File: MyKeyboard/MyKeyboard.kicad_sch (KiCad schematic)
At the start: 64 parts, among them J1 USB_C_Receptacle_USB2.0, J2 USB_C_Receptacle_USB2.0, J3 Conn_01x04, SW1 SW_Push, SW10 SW_Push, SW11 SW_Push, SW12 SW_Push, SW13 SW_Push, SW14 SW_Push, SW15 SW_Push, SW16 SW_Push, SW17 SW_Push, SW18 SW_Push, SW19 SW_Push, SW2 SW_Push, SW20 SW_Push, SW21 SW_Push, SW22 SW_Push, SW23 SW_Push, SW24 SW_Push, SW25 SW_Push, SW26 SW_Push, SW27 SW_Push, SW3 SW_Push, SW4 SW_Push, SW5 SW_Push, SW6 SW_Push, SW7 SW_Push, SW8 SW_Push, SW9 SW_Push, U1 E73-2G4M08S1C, U2 E73-2G4M08S1C

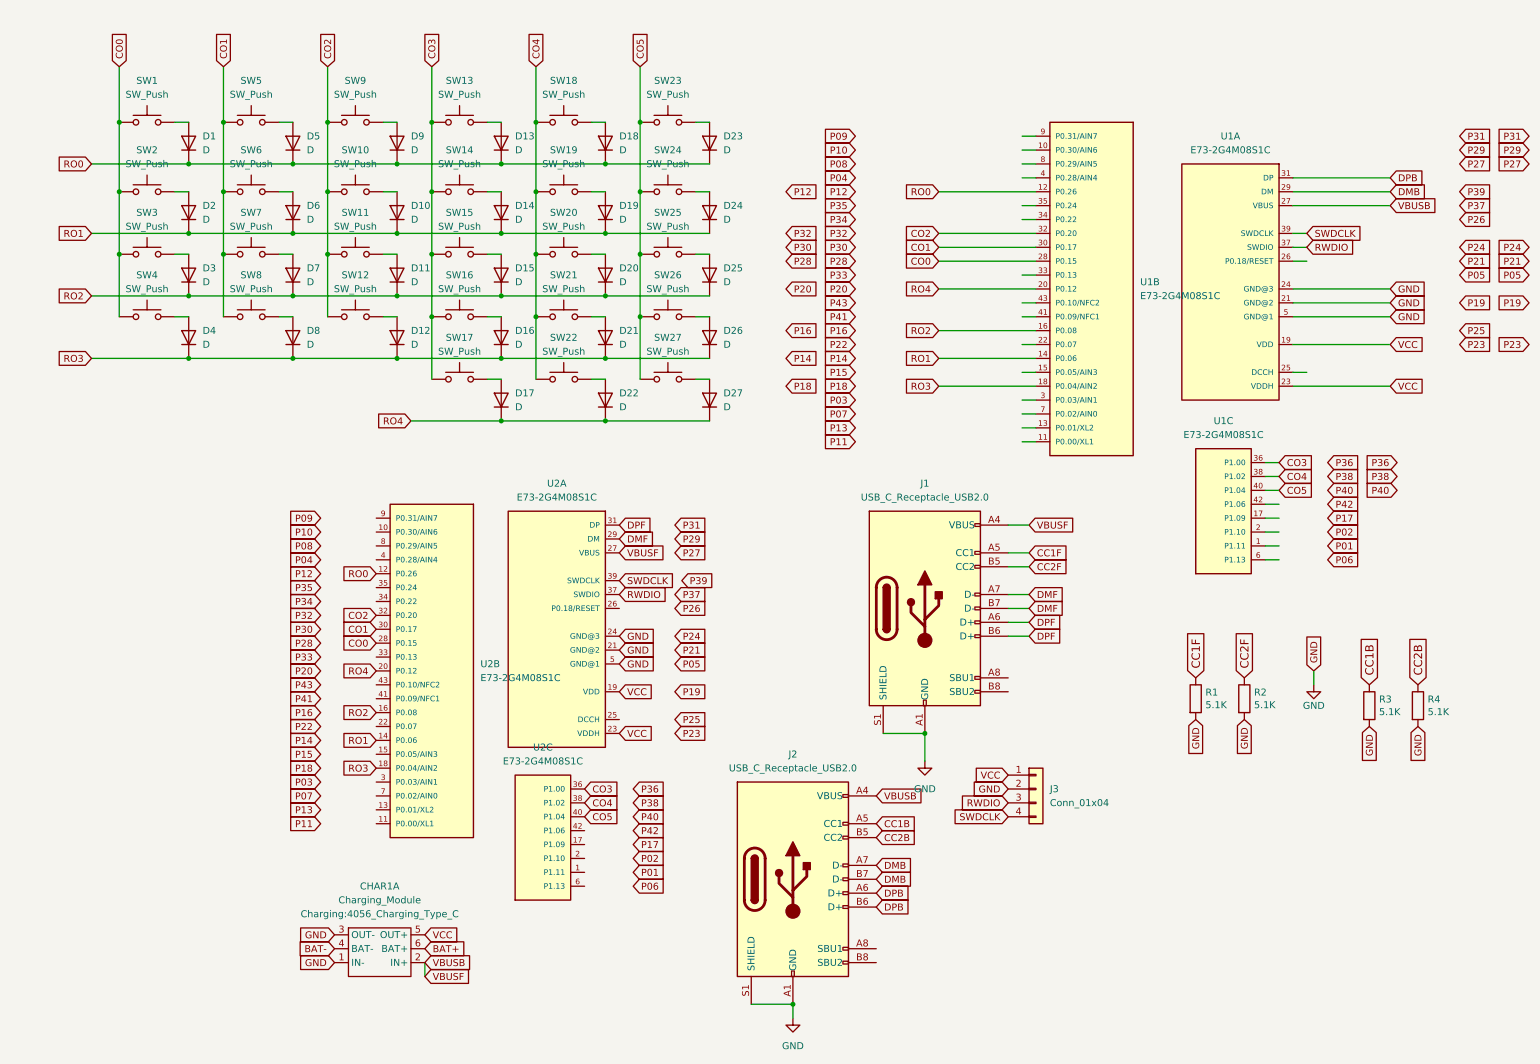
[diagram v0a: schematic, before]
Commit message: update reset btn and wiring
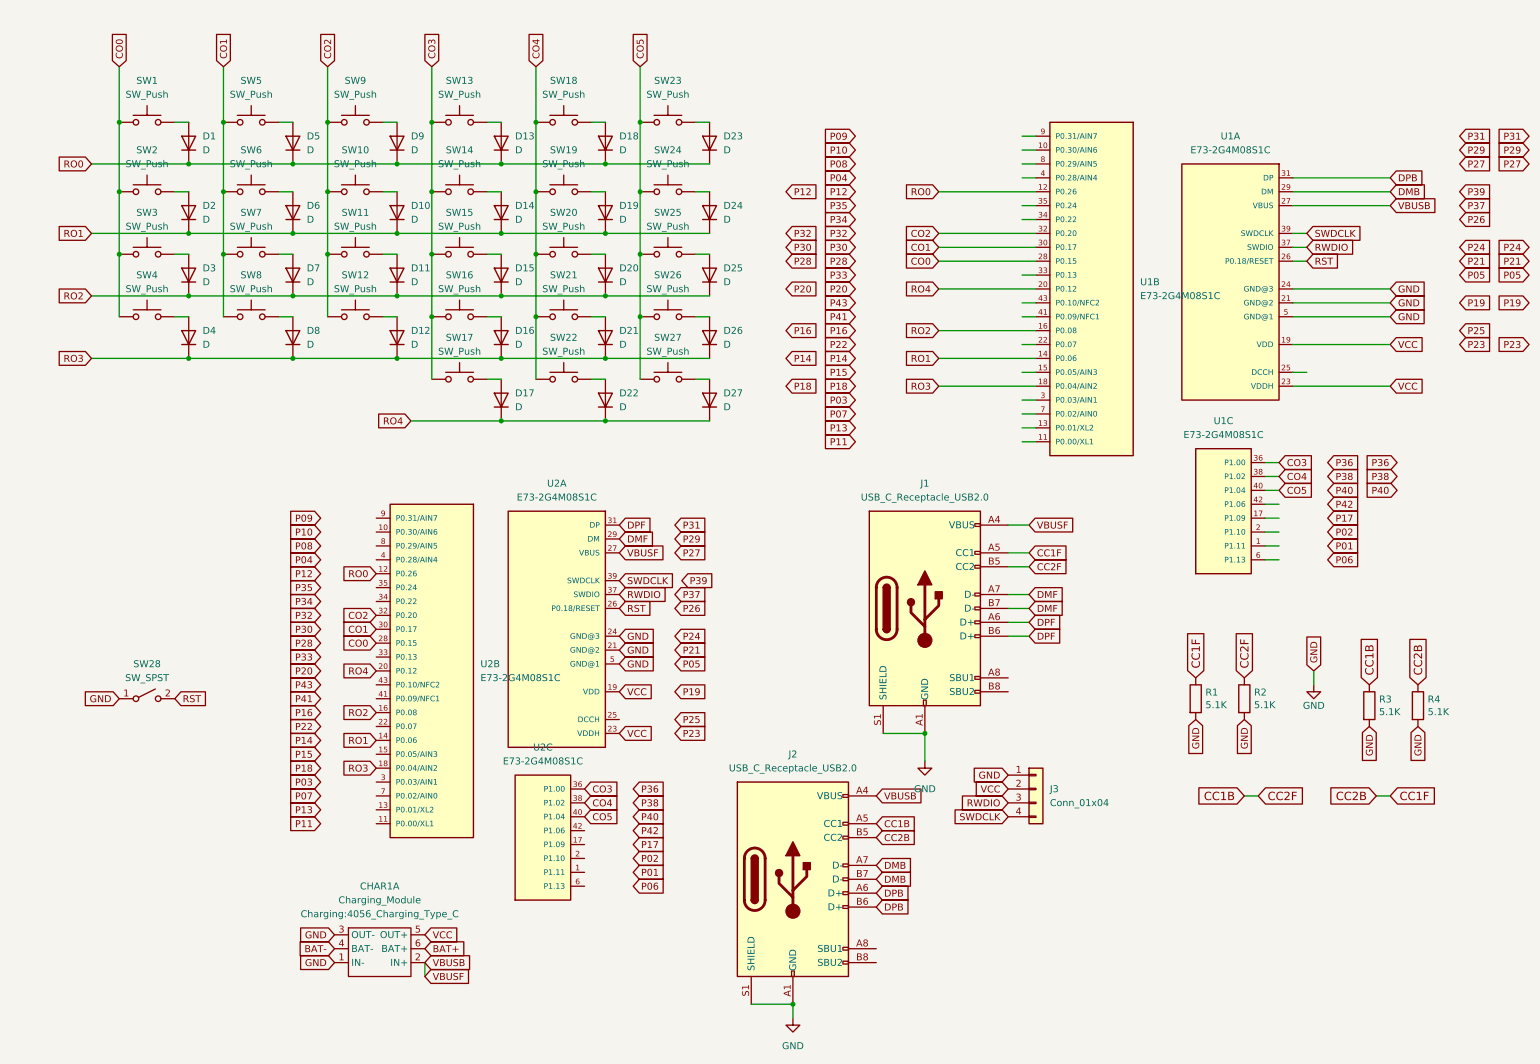
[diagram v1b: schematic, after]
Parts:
- added SW28: SW_SPST, Connector_PinHeader_2.54mm:PinHeader_1x02_P2.54mm_Vertical, symbol Switch:SW_SPST
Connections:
- net CC2B is gone; now on net CC1F: J2.B5 (CC2), R4.1
- net CC2F is gone; now on net CC1B: J1.B5 (CC2), R2.1
- net GND: now also J3.1 (Pin_1), SW28.1 (A); no longer J3.2 (Pin_2)
- net VCC: now also J3.2 (Pin_2); no longer J3.1 (Pin_1)
- net RST: now reaches U1.26 (P0.18/RESET)
- net RST: now also U2.26 (P0.18/RESET), SW28.2 (B)
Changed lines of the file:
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@@
     (stroke (width 0) (type default) (color 0 0 0 0))
   )
+  (wire (pts (xy 261.62 154.94) (xy 264.16 154.94))
+    (stroke (width 0) (type default) (color 0 0 0 0))
+  )
   (wire (pts (xy 246.38 64.77) (xy 264.16 64.77))
     (stroke (width 0) (type default) (color 0 0 0 0))
@@
     (stroke (width 0) (type default) (color 0 0 0 0))
   )
+  (wire (pts (xy 237.49 154.94) (xy 240.03 154.94))
+    (stroke (width 0) (type default) (color 0 0 0 0))
+  )
   (wire (pts (xy 147.32 193.04) (xy 154.94 193.04))
     (stroke (width 0) (type default) (color 0 0 0 0))
@@
     )
   )
+  (global_label "RST" (shape input) (at 123.19 120.65 0) (fields_autoplaced)
+    (effects (font (size 1.27 1.27)) (justify left))
+    (property "Intersheet References" "${INTERSHEET_REFS}" (id 0) (at 129.0502 120.5706 0)
+      (effects (font (size 1.27 1.27)) (justify left) hide)
+    )
+  )
   (global_label "RWDIO" (shape input) (at 194.31 156.21 180) (fields_autoplaced)
     (effects (font (size 1.27 1.27)) (justify right))
@@
     )
   )
-  (global_label "GND" (shape input) (at 194.31 153.67 180) (fields_autoplaced)
+  (global_label "GND" (shape input) (at 194.31 151.13 180) (fields_autoplaced)
     (effects (font (size 1.27 1.27)) (justify right))
-    (property "Intersheet References" "${INTERSHEET_REFS}" (id 0) (at 188.0264 153.7494 0)
+    (property "Intersheet References" "${INTERSHEET_REFS}" (id 0) (at 188.0264 151.2094 0)
       (effects (font (size 1.27 1.27)) (justify right) hide)
     )
@@
     )
   )
+  (global_label "CC1F" (shape input) (at 264.16 154.94 0) (fields_autoplaced)
+    (effects (font (size 1.524 1.524)) (justify left))
+    (property "Intersheet References" "${INTERSHEET_REFS}" (id 0) (at 272.8613 154.8448 0)
+      (effects (font (size 1.524 1.524)) (justify left) hide)
+    )
+  )
   (global_label "P35" (shape input) (at 166.37 46.99 180) (fields_autoplaced)
     (effects (font (size 1.27 1.27)) (justify right))
@@
     )
   )
+  (global_label "RST" (shape input) (at 248.92 57.15 0) (fields_autoplaced)
+    (effects (font (size 1.27 1.27)) (justify left))
+    (property "Intersheet References" "${INTERSHEET_REFS}" (id 0) (at 254.7802 57.0706 0)
+      (effects (font (size 1.27 1.27)) (justify left) hide)
+    )
+  )
   (global_label "P05" (shape input) (at 276.86 59.69 0) (fields_autoplaced)
     (effects (font (size 1.27 1.27)) (justify left))
@@
     )
   )
+  (global_label "CC2F" (shape input) (at 240.03 154.94 0) (fields_autoplaced)
+    (effects (font (size 1.524 1.524)) (justify left))
+    (property "Intersheet References" "${INTERSHEET_REFS}" (id 0) (at 248.7313 155.0352 0)
+      (effects (font (size 1.524 1.524)) (justify left) hide)
+    )
+  )
   (global_label "P02" (shape input) (at 125.73 166.37 0) (fields_autoplaced)
     (effects (font (size 1.27 1.27)) (justify left))
@@
     )
   )
+  (global_label "RST" (shape input) (at 41.91 137.16 0) (fields_autoplaced)
+    (effects (font (size 1.27 1.27)) (justify left))
+    (property "Intersheet References" "${INTERSHEET_REFS}" (id 0) (at 47.7702 137.0806 0)
+      (effects (font (size 1.27 1.27)) (justify left) hide)
+    )
+  )
   (global_label "SWDCLK" (shape input) (at 123.19 115.57 0) (fields_autoplaced)
     (effects (font (size 1.27 1.27)) (justify left))
@@
     )
   )
+  (global_label "CC2B" (shape input) (at 261.62 154.94 180) (fields_autoplaced)
+    (effects (font (size 1.524 1.524)) (justify right))
+    (property "Intersheet References" "${INTERSHEET_REFS}" (id 0) (at 252.701 155.0352 0)
+      (effects (font (size 1.524 1.524)) (justify right) hide)
+    )
+  )
   (global_label "P28" (shape input) (at 153.67 57.15 0) (fields_autoplaced)
     (effects (font (size 1.27 1.27)) (justify left))
@@
     )
   )
+  (global_label "CC1B" (shape input) (at 237.49 154.94 180) (fields_autoplaced)
+    (effects (font (size 1.524 1.524)) (justify right))
+    (property "Intersheet References" "${INTERSHEET_REFS}" (id 0) (at 228.571 155.0352 0)
+      (effects (font (size 1.524 1.524)) (justify right) hide)
+    )
+  )
   (global_label "P38" (shape input) (at 265.43 96.52 180) (fields_autoplaced)
     (effects (font (size 1.27 1.27)) (justify right))
@@
     )
   )
-  (global_label "VCC" (shape input) (at 194.31 151.13 180) (fields_autoplaced)
+  (global_label "VCC" (shape input) (at 194.31 153.67 180) (fields_autoplaced)
     (effects (font (size 1.27 1.27)) (justify right))
-    (property "Intersheet References" "${INTERSHEET_REFS}" (id 0) (at 188.2683 151.0506 0)
+    (property "Intersheet References" "${INTERSHEET_REFS}" (id 0) (at 188.2683 153.5906 0)
       (effects (font (size 1.27 1.27)) (justify right) hide)
     )
@@
     )
   )
+  (global_label "GND" (shape input) (at 31.75 137.16 180) (fields_autoplaced)
+    (effects (font (size 1.27 1.27)) (justify right))
+    (property "Intersheet References" "${INTERSHEET_REFS}" (id 0) (at 25.4664 137.2394 0)
+      (effects (font (size 1.27 1.27)) (justify right) hide)
+    )
+  )
   (global_label "P38" (shape input) (at 252.73 96.52 0) (fields_autoplaced)
     (effects (font (size 1.27 1.27)) (justify left))
@@
     (pin "2")
   )
+  (symbol (lib_id "Switch:SW_SPST") (at 36.83 137.16 0) (unit 1)
+    (in_bom yes) (on_board yes) (fields_autoplaced)
+    (property "Reference" "SW28" (id 0) (at 36.83 130.81 0))
+    (property "Value" "SW_SPST" (id 1) (at 36.83 133.35 0))
+    (property "Footprint" "Connector_PinHeader_2.54mm:PinHeader_1x02_P2.54mm_Vertical" (id 2) (at 36.83 137.16 0)
+      (effects (font (size 1.27 1.27)) hide)
+    )
+    (property "Datasheet" "~" (id 3) (at 36.83 137.16 0)
+      (effects (font (size 1.27 1.27)) hide)
+    )
+    (pin "1")
+    (pin "2")
+  )
   (symbol (lib_id "Device:D") (at 63.5 48.26 90) (unit 1)
     (in_bom yes) (on_board yes) (fields_autoplaced)
@@
       (reference "SW27") (unit 1) (value "SW_Push") (footprint "keyswitches:Kailh_socket_PG1350_reversible")
     )
+    (path "/4581316e-ccbf-413a-9905-eae8f04be4b9"
+      (reference "SW28") (unit 1) (value "SW_SPST") (footprint "Connector_PinHeader_2.54mm:PinHeader_1x02_P2.54mm_Vertical")
+    )
     (path "/973982fc-10aa-472c-ab8b-ef38be799214"

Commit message: finalize standalone keyboard
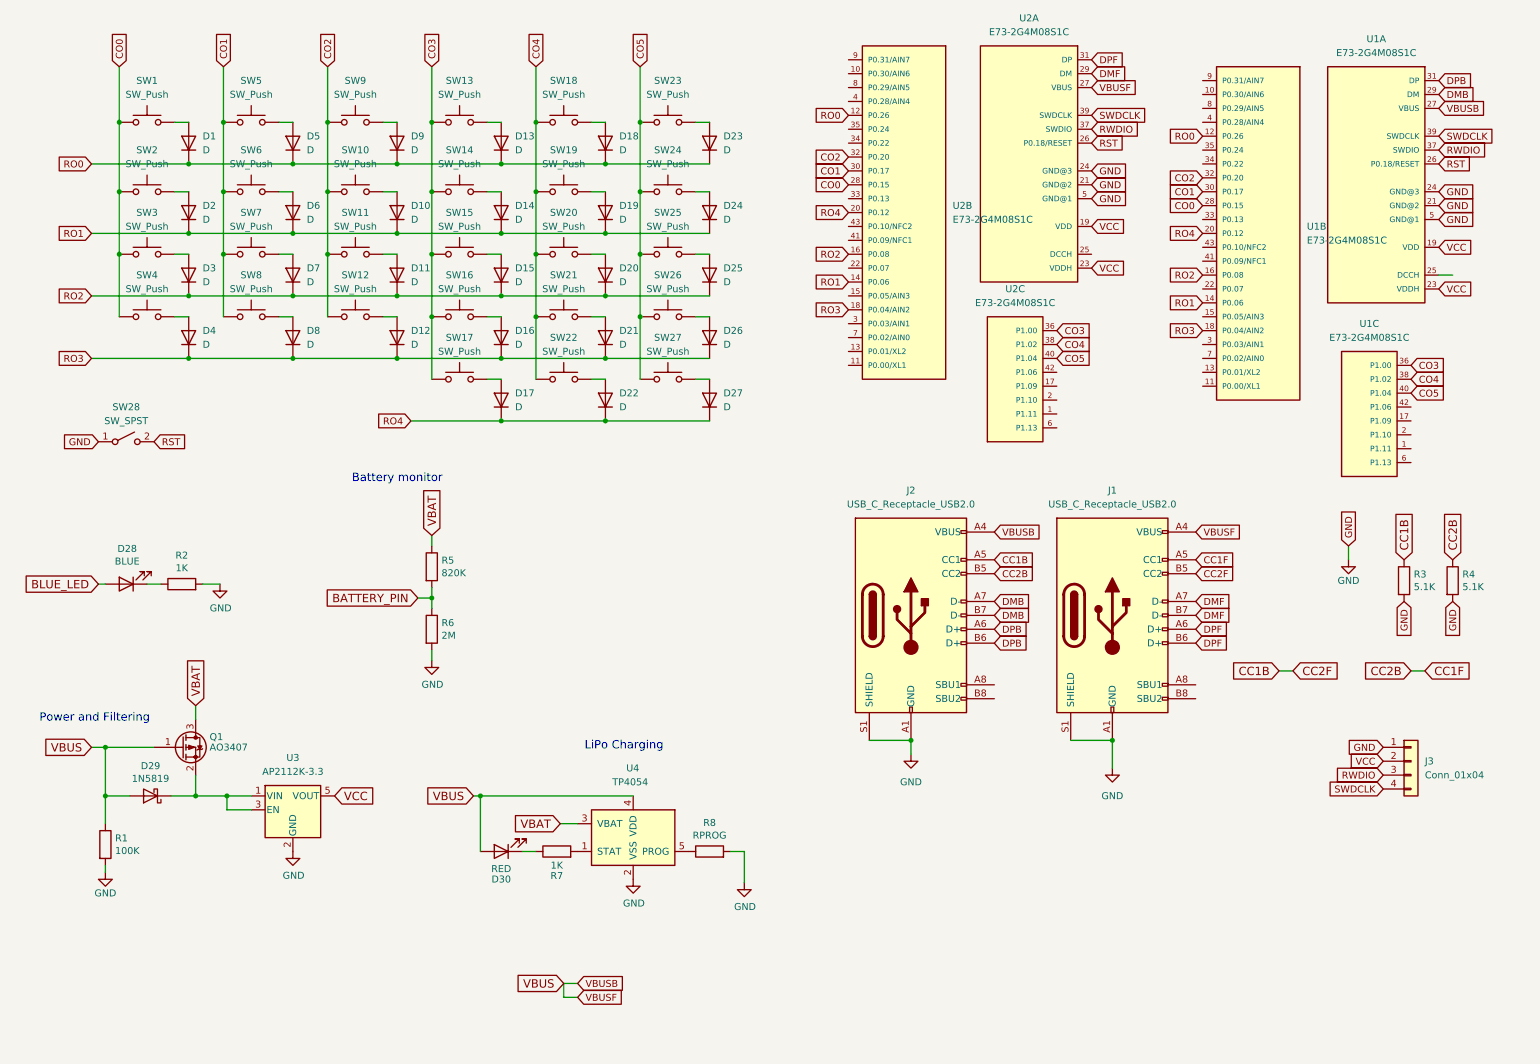
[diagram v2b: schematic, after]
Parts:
- removed CHAR1: Charging_Module, Charging:4056_Charging_Type_C, symbol charging:Charging_Module
- removed R1, R2: 5.1K, Resistor_SMD:R_0603_1608Metric, symbol Device:R
- added D28: BLUE, LED_SMD:LED_0603_1608Metric, symbol Device:LED
- added D29: 1N5819, Diode_SMD:D_SOD-323F, symbol nrfmicro-rescue:MBR0520
- added D30: RED, LED_SMD:LED_0603_1608Metric, symbol Device:LED
- added Q1: AO3407, Package_TO_SOT_SMD:SOT-23, symbol nrfmicro-rescue:BSS83P
- added R1: 100K, Resistor_SMD:R_0603_1608Metric, symbol nrfmicro-rescue:R
- added R2, R7: 1K, Resistor_SMD:R_0603_1608Metric, symbol nrfmicro-rescue:R
- added R5: 820K, Resistor_SMD:R_0603_1608Metric, symbol Device:R
- added R6: 2M, Resistor_SMD:R_0603_1608Metric, symbol Device:R
- added R8: RPROG, Resistor_SMD:R_0603_1608Metric, symbol nrfmicro-rescue:R
- added U3: AP2112K-3.3, Package_TO_SOT_SMD:SOT-23-5, symbol Regulator_Linear:AP2112K-3.3
- added U4: TP4054, Package_TO_SOT_SMD:SOT-23-5, symbol Battery_Management:MCP73832-2-OT
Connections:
- net GND: now also R1.2, R2.2, R6.2, R8.2, U3.2 (GND), U4.2 (VSS)
- net VCC: now also U3.5 (VOUT)
- net VBUSB renamed VBUS
- net VBUS: now also D29.2 (A), D30.2 (A), Q1.1 (G), R1.1, U4.4 (VDD)
- new net: D28.1 (K), R2.1
- new net: D29.1 (K), Q1.2 (S), U3.1 (VIN), U3.3 (EN)
- new net: D30.1 (K), R7.1
- new net: R7.2, U4.1 (STAT)
- new net: R8.1, U4.5 (PROG)
- new net BATTERY_PIN: R5.2, R6.1
- new net BLUE_LED: D28.2 (A)
- new net VBAT: Q1.3 (D), R5.1, U4.3 (VBAT)
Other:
- note added: "Battery monitor"
- note added: "LiPo Charging"
- note added: "Power and Filtering"
- moved on the sheet: J1, J2, J3, R3, R4, SW28, U1A, U1B, U1C, U2A, U2B, U2C
